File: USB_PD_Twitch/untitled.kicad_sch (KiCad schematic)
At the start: 19 parts, among them Q3 Q_PMOS_GSD, U12 CXP0650-220M-AG(22UH), U2 NDP1360KC, U3 XPD738B20

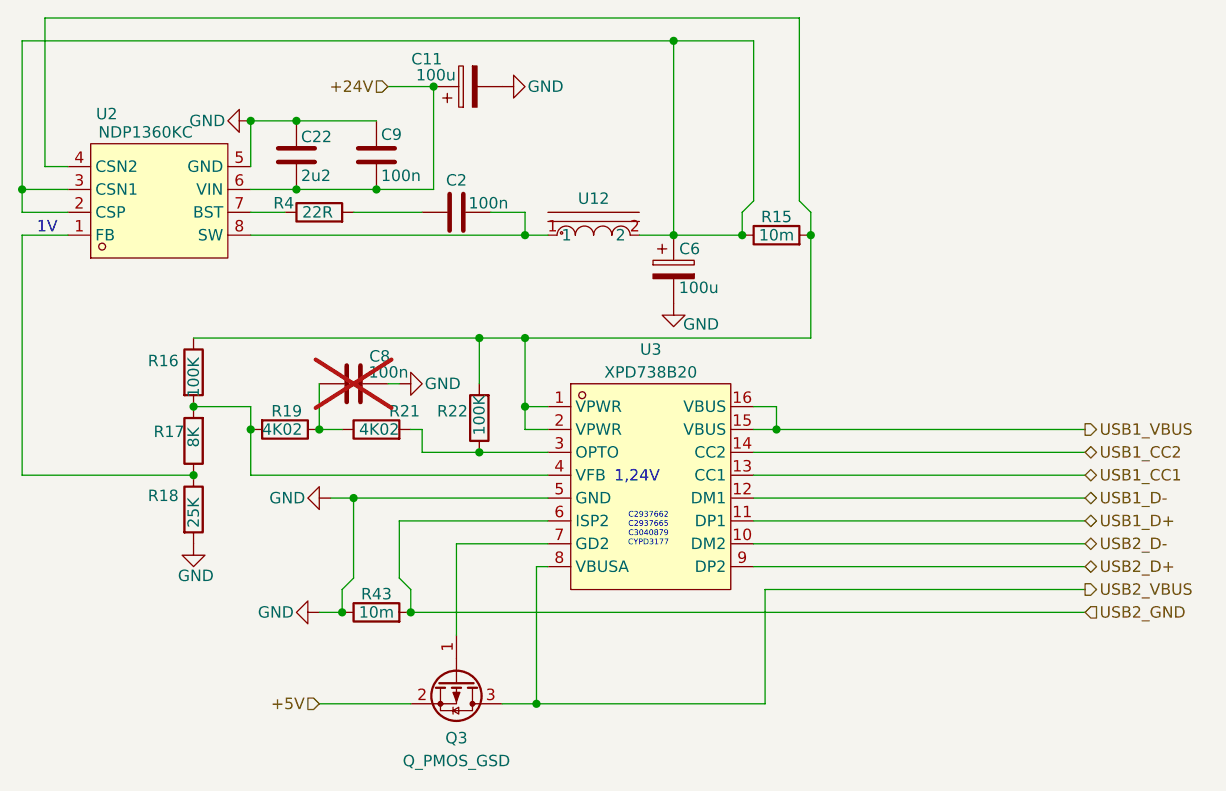
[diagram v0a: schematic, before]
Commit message: add nev versions. (usb c and displayport working)
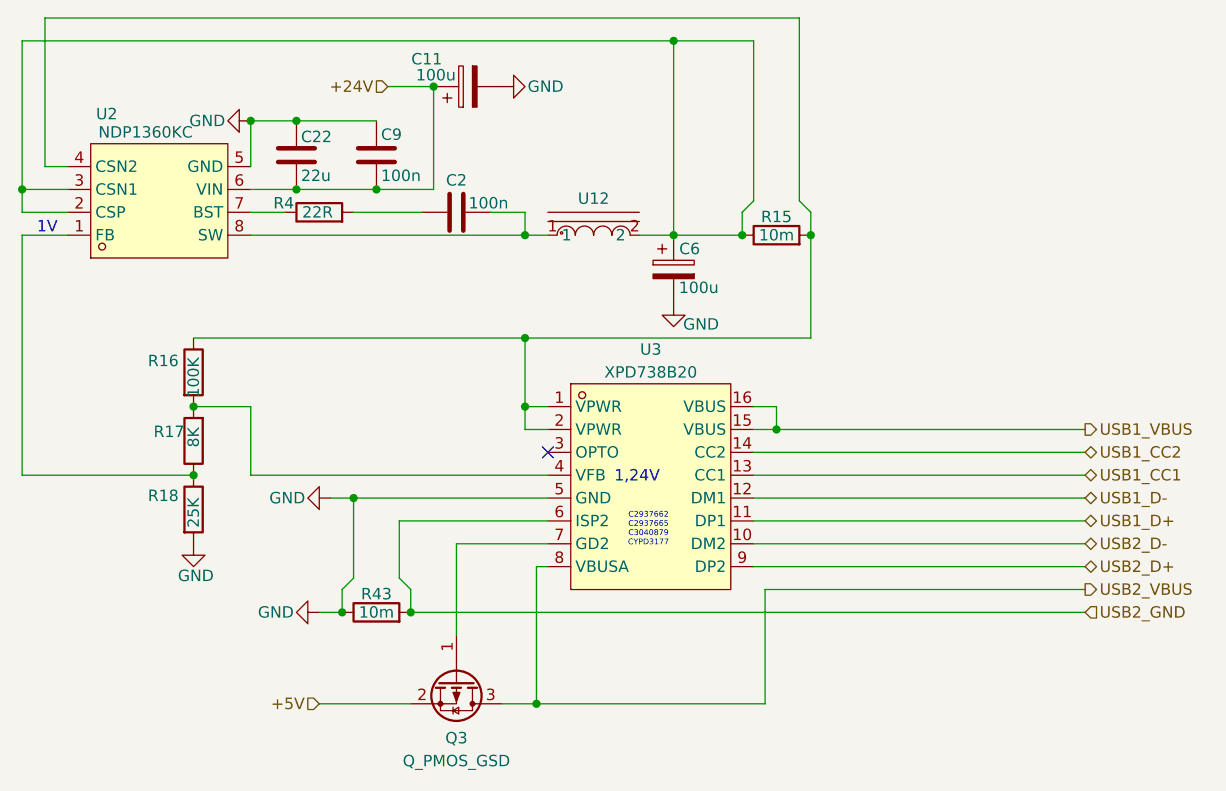
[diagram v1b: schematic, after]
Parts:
- removed C8: 100n, Capacitor_SMD:C_0603_1608Metric, symbol Device:C
- removed R19, R21: 4K02, Resistor_SMD:R_0402_1005Metric, symbol Device:R
- removed R22: 100K, Resistor_SMD:R_0402_1005Metric, symbol Device:R
- C11, C6: footprint Capacitor_SMD:CP_Elec_6.3x7.7 -> Capacitor_SMD:CP_Elec_8x10
- C22: value 2u2 -> 22u
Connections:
- no-connect marks 0 -> 1
